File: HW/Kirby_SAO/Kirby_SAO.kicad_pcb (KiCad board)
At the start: 2 copper layers, 9 parts, among them X1 Badgelife_sao_connector_v169b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

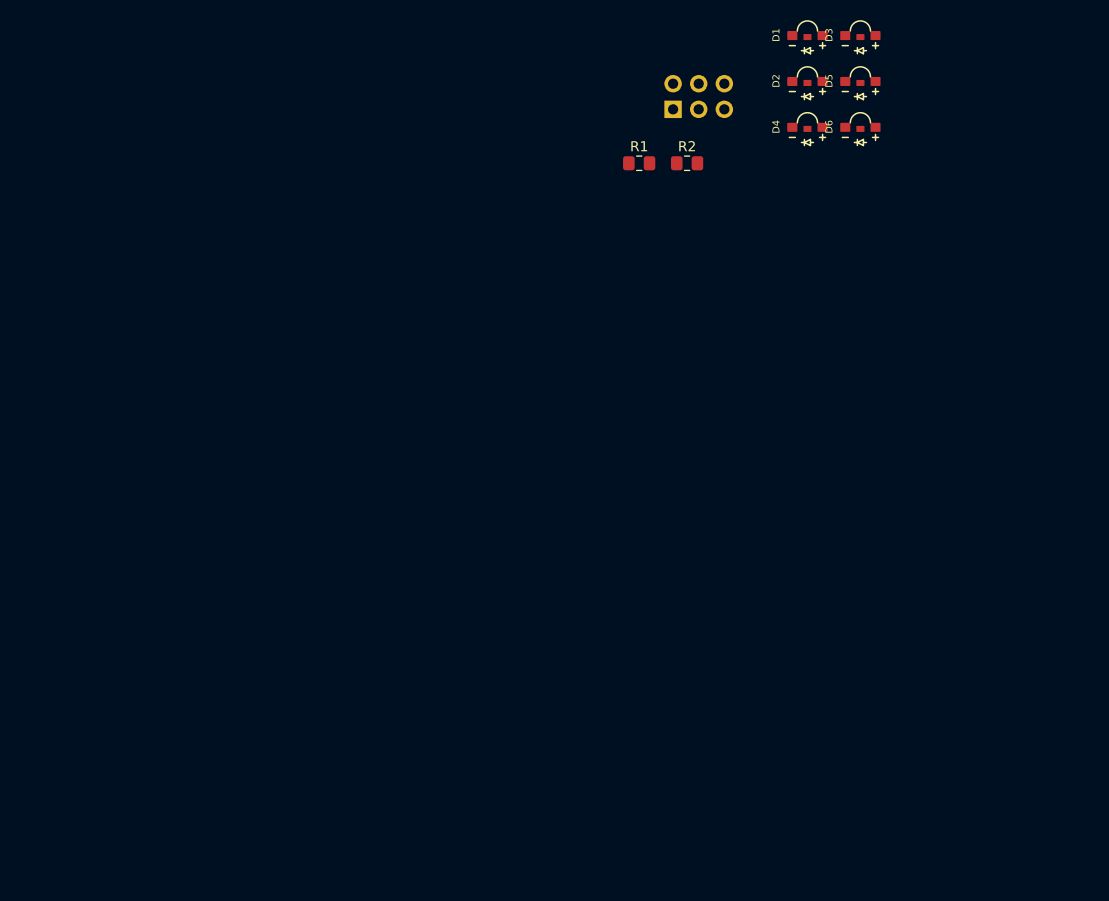
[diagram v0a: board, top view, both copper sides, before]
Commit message: added footprints
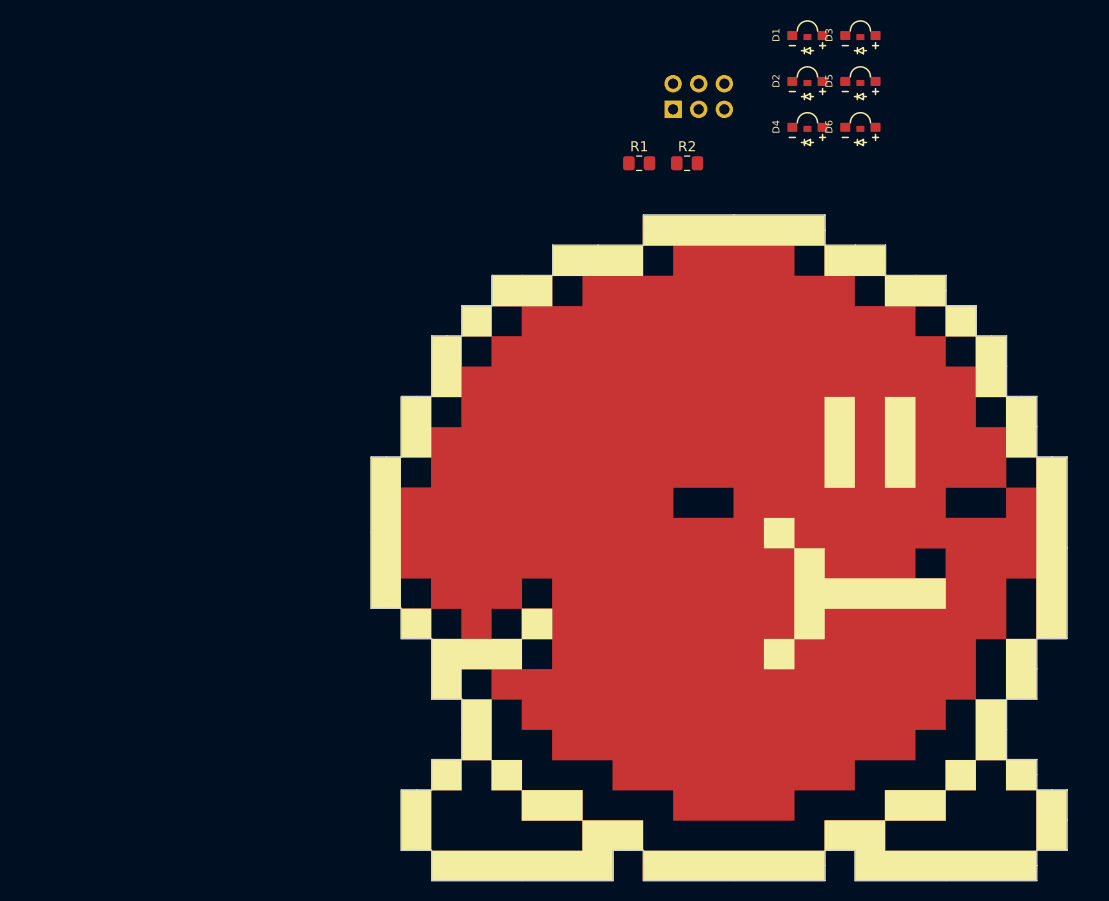
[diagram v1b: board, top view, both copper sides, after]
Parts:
- added G***: F.Silk, Kirby_SAO:F.Silk_g4158, F.Cu at (100.0, 100.0)
- added G***: F.Mask, Kirby_SAO:F.Mask_g4156, F.Cu at (100.0, 100.0)
- added G***: F.Cu, Kirby_SAO:F.Cu_g4154, F.Cu at (100.0, 100.0)
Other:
- board outline added: 69 x 66 mm

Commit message: moving around LEDs
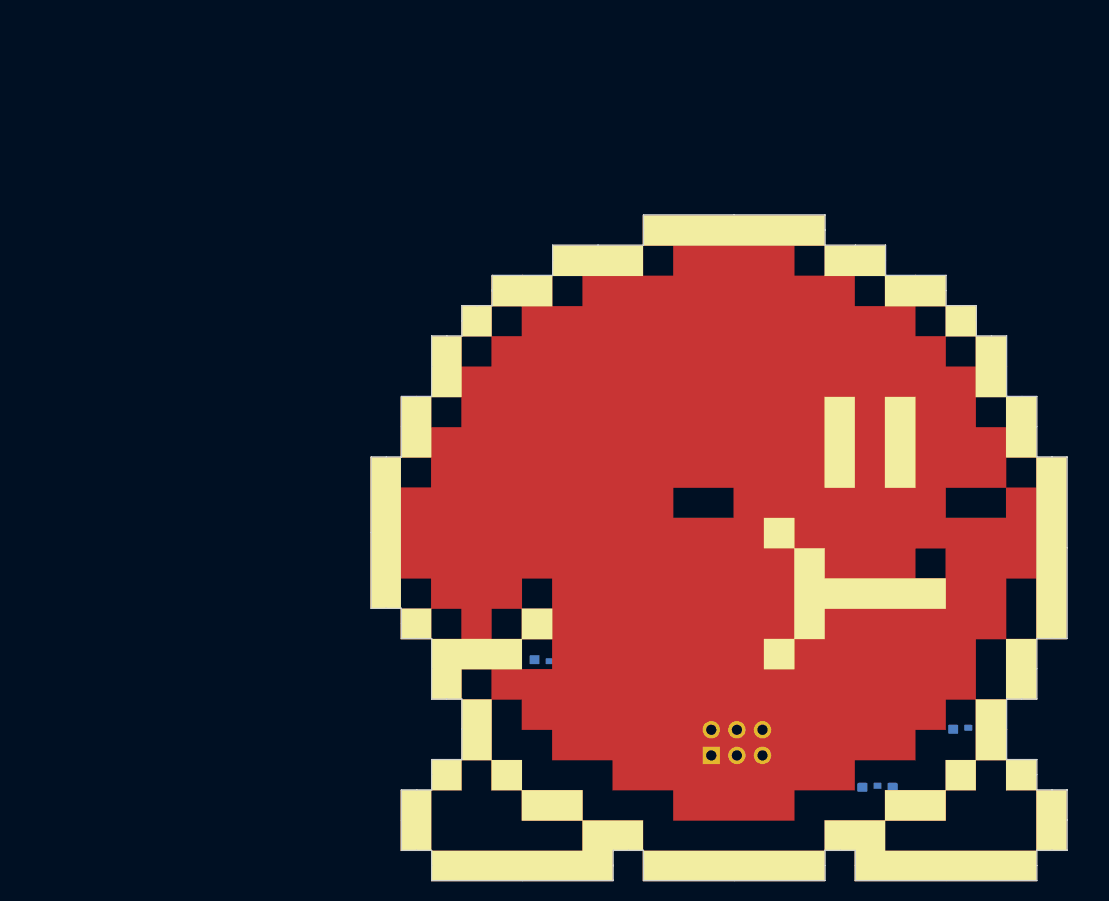
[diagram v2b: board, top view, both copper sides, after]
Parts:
- D1, D2, D3, D4, D5, D6, R1, R2: moved to B.Cu
- moved D1 66.9 mm to (83.2, 111.0), turned to 180 degrees
- moved D6 65.5 mm to (115.8, 123.8)
- moved X1 64.2 mm to (101.8, 119.2)
- moved D4 61.9 mm to (124.8, 118.0)
- moved D3 55.1 mm to (85.5, 96.2)
- moved R2 49.7 mm to (109.0, 110.0), turned to 90 degrees
- moved R1 49.0 mm to (101.0, 110.0), turned to 90 degrees
- moved D5 46.5 mm to (125.5, 98.8), turned to 180 degrees
- moved D2 46.2 mm to (98.5, 98.8), turned to 180 degrees

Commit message: stuff changed
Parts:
- moved D4 10.0 mm to (134.8, 118.8)
- moved D2 1.35 mm to (99.0, 100.0)
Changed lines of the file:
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@@
     (35 F.Paste user hide)
     (36 B.SilkS user)
-    (37 F.SilkS user hide)
+    (37 F.SilkS user)
     (38 B.Mask user)
     (39 F.Mask user)
@@
   )
   (module Kirby_SAO:1204_SIDE_VIEW_LED (layer B.Cu)
-    (at 98.5 98.75 180)
+    (at 99 100 180)
     (fp_text reference D2 (at -3.1 0 270) (layer B.SilkS)
       (effects (font (size 0.7 0.7) (thickness 0.15)) (justify mirror))
@@
   )
   (module Kirby_SAO:1204_SIDE_VIEW_LED (layer B.Cu)
-    (at 124.75 118)
+    (at 134.75 118.75)
     (fp_text reference D4 (at -3.1 0 -90) (layer B.SilkS)
       (effects (font (size 0.7 0.7) (thickness 0.15)) (justify mirror))

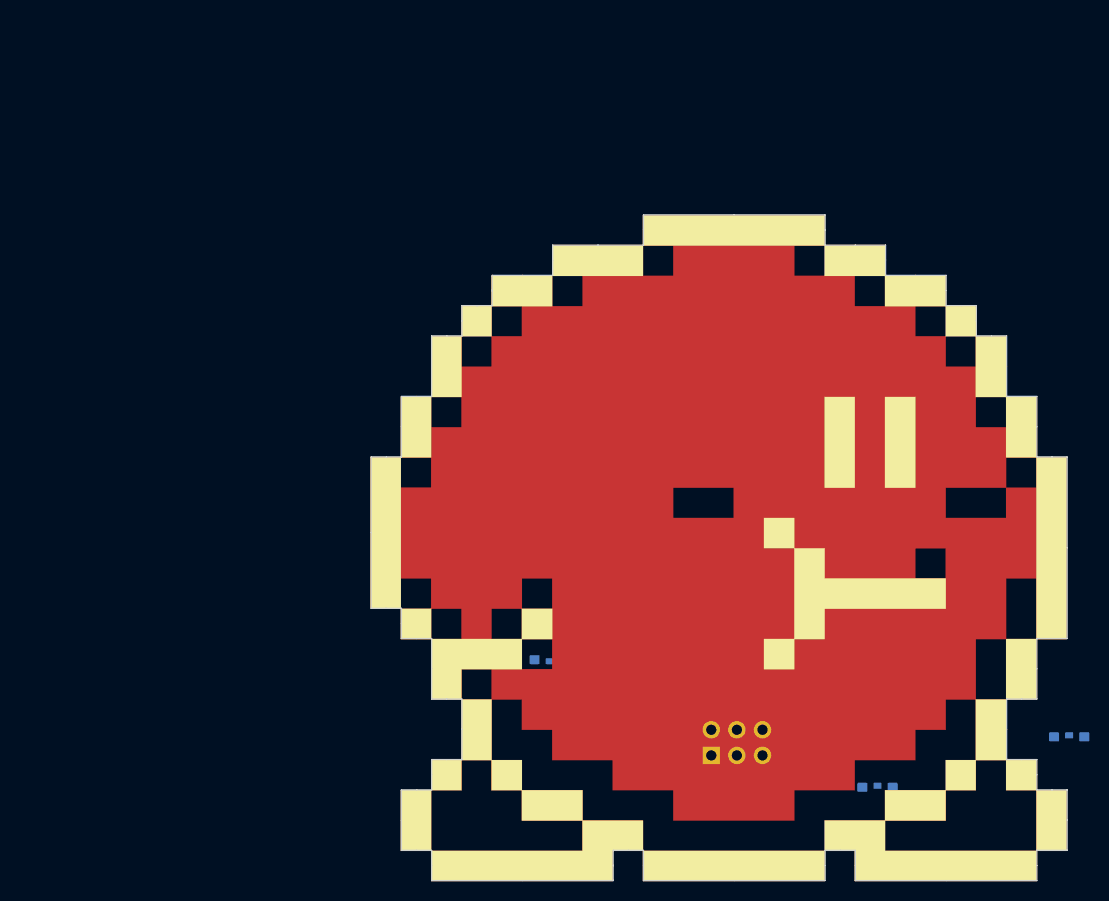
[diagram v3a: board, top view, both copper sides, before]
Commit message: Fixed wiring in schematic, generate netlist. Added 3D model for LED. Updated footprints for board layers. impported netlist and footprints to PCBnew
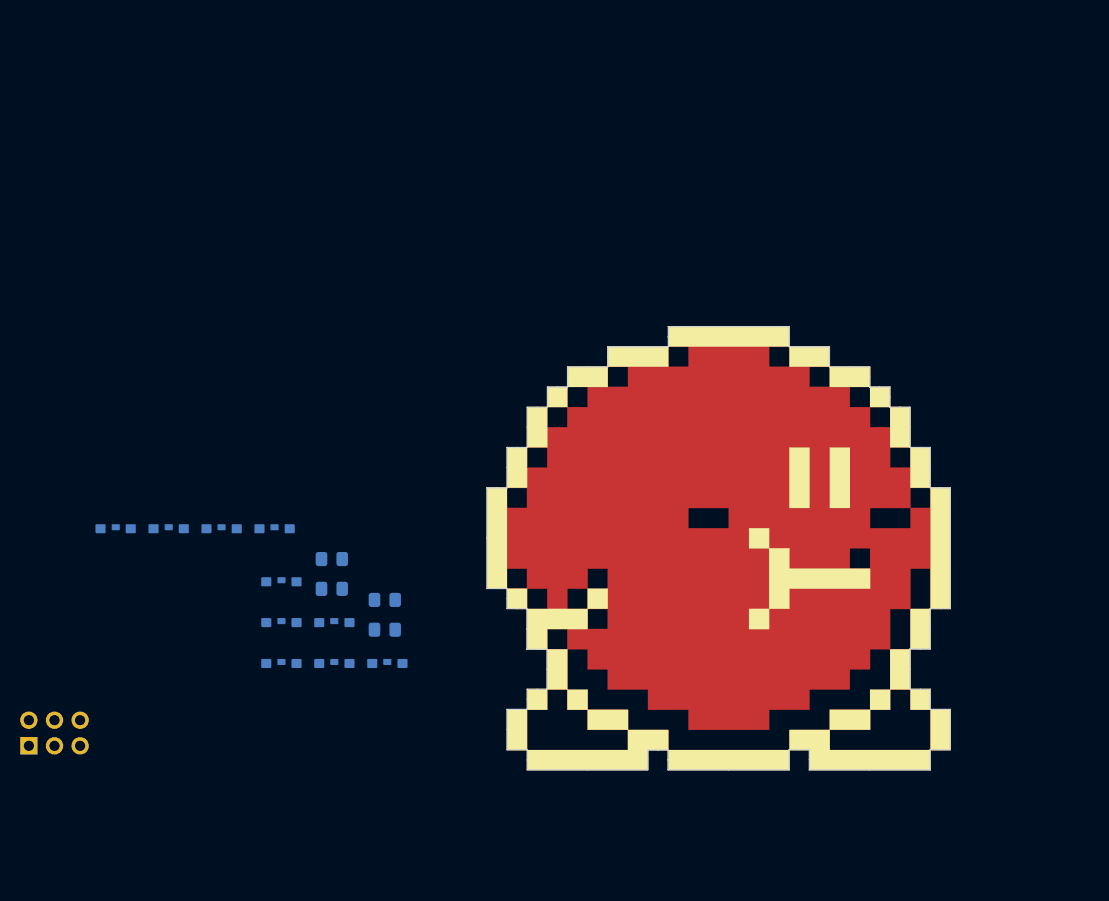
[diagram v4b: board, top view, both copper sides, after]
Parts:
- added D10: LED, Kirby_SAO:1204_SIDE_VIEW_LED, B.Cu at (56.0, 98.1)
- added D7: LED, Kirby_SAO:1204_SIDE_VIEW_LED, B.Cu at (56.7, 103.4)
- added D8: LED, Kirby_SAO:1204_SIDE_VIEW_LED, B.Cu at (61.9, 107.4)
- added D9: LED, Kirby_SAO:1204_SIDE_VIEW_LED, B.Cu at (67.2, 111.5)
- added G***: B.Mask, Kirby_SAO:B.Mask_g4150, F.Cu at (100.0, 100.0)
- added R3: 100R, Resistor_SMD:R_0805_2012Metric_Pad1.15x1.40mm_HandSolder, B.Cu at (61.7, 101.1)
- added R4: 100R, Resistor_SMD:R_0805_2012Metric_Pad1.15x1.40mm_HandSolder, B.Cu at (66.9, 105.1)
- G***: value F.Silk -> LOGO
- R1, R2: value 51R -> 100R
- moved D4 78.9 mm to (56.7, 107.4)
- moved D6 69.9 mm to (50.7, 98.1)
- moved X1 67.7 mm to (34.1, 118.3)
- moved D5 64.9 mm to (61.9, 111.5), turned to 0 degrees
- moved D1 44.9 mm to (40.2, 98.1), turned to 0 degrees
- moved D2 43.9 mm to (56.7, 111.5), turned to 0 degrees
- moved R2 42.1 mm to (66.9, 108.1), turned to 0 degrees
- moved D3 40.1 mm to (45.5, 98.1)
- moved R1 39.8 mm to (61.7, 104.0), turned to 0 degrees
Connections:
- D4 pad 2: Net-(D4-Pad2) -> Net-(D1-Pad2)
- D5 pad 2: Net-(D4-Pad2) -> Net-(D1-Pad2)
- D6 pad 2: Net-(D4-Pad2) -> Net-(D10-Pad2)
- R2 pad 2: Net-(D4-Pad2) -> Net-(D1-Pad2)
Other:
- board size 69 x 66 mm -> 45.9 x 43.9 mm

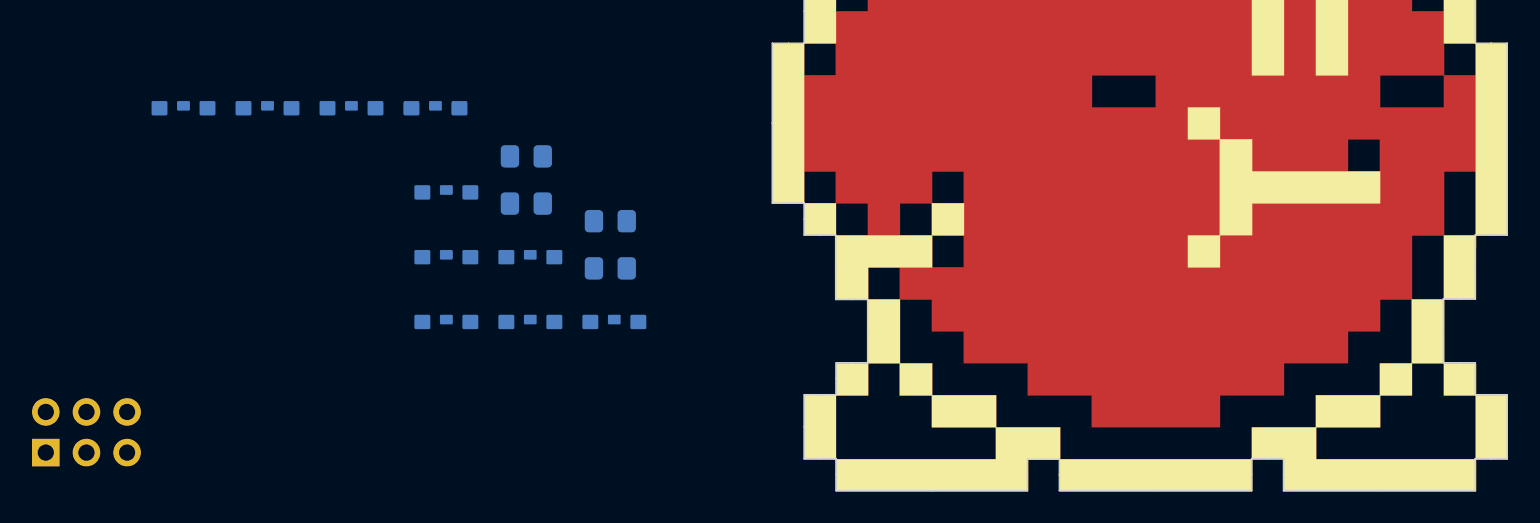
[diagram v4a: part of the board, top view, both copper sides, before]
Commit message: Places LEDs Added B.Cu keepout
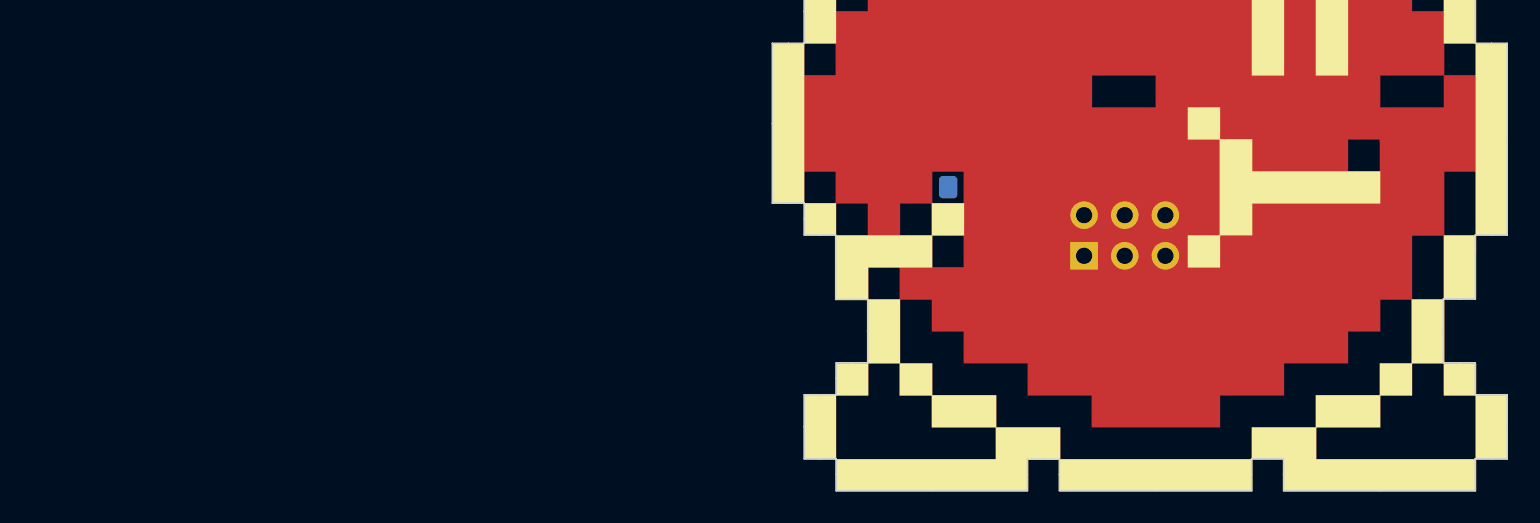
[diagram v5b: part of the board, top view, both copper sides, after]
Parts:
- moved D6 66.3 mm to (117.0, 99.8), turned to 180 degrees
- moved X1 66.1 mm to (99.0, 106.0)
- moved D10 60.1 mm to (115.2, 108.2), turned to 45 degrees
- moved D1 58.8 mm to (99.0, 99.8), turned to 180 degrees
- moved D8 58.1 mm to (118.5, 120.4), turned to 180 degrees
- moved R3 49.4 mm to (111.0, 98.0)
- moved D7 48.3 mm to (103.2, 116.0), turned to 45 degrees
- moved D9 44.3 mm to (111.5, 112.0), turned to 45 degrees
- moved R4 44.1 mm to (111.0, 103.0)
- moved D3 44.1 mm to (83.5, 120.4), turned to 180 degrees
- moved D5 37.2 mm to (98.9, 116.0), turned to 315 degrees
- moved D2 34.6 mm to (91.2, 112.5)
- moved D4 33.1 mm to (89.8, 109.0), turned to 270 degrees
- moved R1 26.1 mm to (87.0, 98.0)
- moved R2 20.7 mm to (87.0, 103.0)
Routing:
- net VCC: track 0.00 -> 5.00 mm
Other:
- net class Default: clearance 0.2 -> 0.1778; trace_width 0.25 -> 0.1778
- rule trace_clearance: 0.2 -> 0.1778
- rule trace_min: 0.2 -> 0.1778
